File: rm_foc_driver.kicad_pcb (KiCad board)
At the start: 4 copper layers, 54.6 x 61.8 mm, 71 parts, among them J1 SWD, J2 SENSOR, J3 UART, J4 TMC4671, J5 PWM, J6 Conn_01x02, J7 CURRENT_SENSE, J8 Conn_01x03, Q1 IRF7580M, Q2 IRF7580M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

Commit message: Not complete yet
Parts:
- removed C1 (x2): 10uF, Capacitor_SMD:C_0603_1608Metric
- removed C14, C18, C19, C20: 100nF, Capacitor_SMD:C_0603_1608Metric
- removed C17: 1uF, Capacitor_SMD:C_0603_1608Metric
- removed C21: 2.2nF, Capacitor_SMD:C_0603_1608Metric
- removed J7: CURRENT_SENSE, Connector_PinHeader_2.54mm:PinHeader_1x02_P2.54mm_Vertical
- removed U5: AS5047D, Package_SO:TSSOP-14_4.4x5mm_P0.65mm
- added D4: DIODE, Diode_SMD:D_SMA, F.Cu at (169.3, 100.8)
- added D5: DIODE, Diode_SMD:D_SMA, F.Cu at (164.5, 100.8)
- added D6: DIODE, Diode_SMD:D_SMA, F.Cu at (159.6, 100.9)
- added R12: 200k, Resistor_SMD:R_0603_1608Metric, F.Cu at (80.9, 157.8)
- added R13: 10R, Resistor_SMD:R_0603_1608Metric, F.Cu at (156.2, 94.0)
- added R14: 10R, Resistor_SMD:R_0603_1608Metric, F.Cu at (162.1, 94.0)
- added R15: 10R, Resistor_SMD:R_0603_1608Metric, F.Cu at (152.4, 94.0)
- added R16: 10R, Resistor_SMD:R_0603_1608Metric, F.Cu at (160.0, 94.0)
- added R17: 10R, Resistor_SMD:R_0603_1608Metric, F.Cu at (148.6, 93.9)
- added R18: 10R, Resistor_SMD:R_0603_1608Metric, F.Cu at (158.1, 94.0)
- added U6: INA2180, Package_SO:VSSOP-8_3.0x3.0mm_P0.65mm, F.Cu at (169.4, 93.4)
- added U7: MT6701, Package_SO:SOP-8_3.9x4.9mm_P1.27mm, B.Cu at (165.1, 101.0)
- C10: value 1uF -> 100nF; moved to F.Cu
- C12, C13: value 1uF -> 100nF
- C15: value 2.2uF -> 1uF
- C16: value 4.7uF -> 1uF; footprint Capacitor_SMD:C_0805_2012Metric -> Capacitor_SMD:C_0603_1608Metric
- C2, C24, C25, C26, C27, C29, C30, C31, C32, C33, C34, C35, C36, C37: moved to F.Cu
- R9: value 1R -> 200k
- U4: value DRV8303 -> EG2133; footprint Package_SO:TSSOP-48_6.1x12.5mm_P0.5mm -> Package_SO:TSSOP-20_4.4x6.5mm_P0.65mm
- moved J1 143.9 mm to (45.6, 152.0), turned to 0 degrees
- moved C32 134.3 mm to (54.8, 176.0), turned to 0 degrees
- moved C27 124.9 mm to (50.4, 176.0), turned to 0 degrees
- moved C34 122.6 mm to (59.1, 174.2)
- moved J2 122.1 mm to (28.1, 170.2), turned to 0 degrees
- moved J4 121.3 mm to (32.8, 152.8), turned to 0 degrees
- moved C24 119.4 mm to (37.3, 161.1), turned to 0 degrees
- moved C16 116.5 mm to (59.1, 176.8), turned to 0 degrees
- moved J3 115.3 mm to (60.9, 135.1), turned to 0 degrees
- moved D2 112.3 mm to (59.6, 168.5), turned to 0 degrees
- moved C31 112.2 mm to (68.2, 163.7), turned to 0 degrees
- moved C25 111.6 mm to (58.4, 171.5), turned to 0 degrees
- moved D1 111.4 mm to (63.6, 168.5), turned to 0 degrees
- moved Y1 109.3 mm to (76.8, 153.8), turned to 0 degrees
- moved C33 106.8 mm to (70.1, 151.7), turned to 0 degrees
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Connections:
- C10 pad 1: +3.3V -> Net-(C10-Pad1)
- C10 pad 2: GND -> /SH_A
- C12 pad 2: GND -> /SH_B
- C13 pad 2: GND -> /SH_C
- C15 pad 1: GND -> +5V
- C15 pad 2: Net-(C15-Pad2) -> GND
- C16 pad 1: +12V -> +5V
- R9 pad 1: Net-(R9-Pad1) -> +5V
- R9 pad 2: GND -> Net-(R9-Pad2)
- U4 pad 1: unconnected-(U4-Pad1) -> /PWM1
- U4 pad 12: /EN_GATE -> /SH_A
- U4 pad 13: /PWM1 -> Net-(U4-Pad13)
- U4 pad 14: /PWM2 -> Net-(C10-Pad1)
- U4 pad 15: /PWM3 -> /SH_B
- U4 pad 16: /PWM4 -> Net-(U4-Pad16)
- U4 pad 17: /PWM5 -> Net-(C12-Pad1)
- U4 pad 18: /PWM6 -> /SH_C
- U4 pad 19: Net-(C12-Pad1) -> Net-(U4-Pad19)
- U4 pad 2: unconnected-(U4-Pad2) -> /PWM2
- U4 pad 20: +3.3V -> Net-(C13-Pad1)
- U4 pad 3: Net-(R9-Pad1) -> /PWM3
- U4 pad 4: /CS1 -> /PWM4
- U4 pad 5: /MOSI -> /PWM5
- U4 pad 6: /MISO -> /PWM6
- U4 pad 7: /SCLK -> +5V
- U4 pad 8: /DC_CAL -> GND
- U4 pad 9: Net-(C15-Pad2) -> Net-(U4-Pad9)
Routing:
- net +3.3V: track 121.5 -> 0.00 mm, vias 7 -> 0
- net +5V: track 114.5 -> 32.0 mm, vias 4 -> 1
- net GND: track 66.1 -> 0.00 mm, vias 58 -> 0
- net /SCLK: track 64.6 -> 0.00 mm, vias 2 -> 0
- net /MISO: track 61.8 -> 0.00 mm, vias 2 -> 0
- net /MOSI: track 57.5 -> 0.00 mm, vias 2 -> 0
- net /CS1: track 47.3 -> 0.00 mm, vias 2 -> 0
- net /Encoder_I: track 41.9 -> 0.00 mm
- net /Encoder_B: track 36.7 -> 0.00 mm
- net /Encoder_A: track 35.7 -> 0.00 mm
- net /SL_A: track 34.0 -> 0.00 mm, vias 22 -> 24
- net /DC_CAL: track 33.7 -> 0.00 mm, vias 2 -> 0
- net /SWDIO: track 27.7 -> 0.00 mm, vias 2 -> 0
- net /EN_GATE: track 27.7 -> 0.00 mm, vias 2 -> 0
- net Net-(D1-Pad1): track 26.3 -> 0.00 mm
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- added copper zone on B.Cu, net /SL_A
- added copper zone on B.Cu, net /SL_B
- removed copper zone on B.Cu, net +12V
- removed copper zone on B.Cu, net /SH_A
- removed copper zone on In1.Cu, net /SH_A
- removed copper zone on B.Cu, net /SH_B
- removed copper zone on In1.Cu, net /SH_B
- removed copper zone on B.Cu, net /SH_C
- removed copper zone on In1.Cu, net /SH_C
- removed copper zone on B.Cu, net GND
- removed copper zone on F.Cu, net GND
- removed copper zone on In1.Cu, net GND
- removed copper zone on In2.Cu, net GND
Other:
- board size 54.6 x 61.8 mm -> 70 x 70 mm

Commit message: new verson of pcb.ready to print
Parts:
- removed J2: SENSOR, Connector_PinHeader_2.54mm:PinHeader_1x03_P2.54mm_Vertical
- removed R12, R9: 200k, Resistor_SMD:R_0603_1608Metric
- C16: moved to B.Cu
- D3, D4, D5, D6: footprint Diode_SMD:D_SMA -> Diode_SMD:D_SOD-123
- moved C32 143.3 mm to (170.2, 91.0), turned to -90 degrees
- moved C27 135.1 mm to (155.5, 91.1), turned to -90 degrees
- moved C24 132.7 mm to (150.1, 91.1), turned to -90 degrees
- moved C15 131.9 mm to (178.9, 108.8), turned to -90 degrees
- moved C16 130.8 mm to (164.6, 99.4), turned to 180 degrees
- moved D2 122.1 mm to (172.1, 121.3), turned to 180 degrees
- moved C31 121.5 mm to (165.6, 91.0), turned to -90 degrees
- moved C34 120.3 mm to (168.5, 124.3), turned to 180 degrees
- moved C25 120.0 mm to (147.6, 91.1), turned to -90 degrees
- moved D1 119.7 mm to (172.2, 118.2), turned to 180 degrees
- moved J4 118.3 mm to (148.6, 128.7), turned to -128 degrees
- moved J1 118.1 mm to (161.5, 129.8), turned to -90 degrees
- moved C33 115.1 mm to (167.9, 91.0), turned to -90 degrees
- moved J3 113.9 mm to (174.7, 130.0), turned to -90 degrees
- moved C29 113.6 mm to (157.9, 91.1), turned to -90 degrees
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- renumbered C22 to C
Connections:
- C11 pad 1: /OSC_IN -> /OSC_OUT
- C9 pad 1: /OSC_OUT -> /OSC_IN
- J4 pad 4: /CS3 -> /CS2
- U3 pad 18: unconnected-(U3-Pad18) -> /ADC1
- U3 pad 19: unconnected-(U3-Pad19) -> /MODE
- U3 pad 29: /CS3 -> unconnected-(U3-Pad29)
- U7 pad 2: Net-(R9-Pad2) -> /MODE
- U7 pad 3: unconnected-(U7-Pad3) -> /ADC1
- U7 pad 6: unconnected-(U7-Pad6) -> /MISO
- U7 pad 7: unconnected-(U7-Pad7) -> /SCLK
- U7 pad 8: Net-(R12-Pad1) -> /CS1
- Y1 pad 1: /OSC_OUT -> /OSC_IN
- Y1 pad 3: /OSC_IN -> /OSC_OUT
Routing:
- net +3.3V: track 0.00 -> 94.1 mm, vias 0 -> 6
- net +5V: track 32.0 -> 115.0 mm, vias 1 -> 8
- net /SL_A: track 0.00 -> 51.1 mm, vias 24 -> 16
- net /SCLK: track 0.00 -> 50.2 mm
- net /MISO: track 0.00 -> 50.2 mm
- net /SL_B: track 0.00 -> 42.8 mm, vias 24 -> 16
- net GND: track 0.00 -> 37.6 mm, vias 0 -> 74
- net /GL_C: track 0.00 -> 33.7 mm, vias 0 -> 2
- net /MODE: track 0.00 -> 28.2 mm, vias 0 -> 2
- net /ADC1: track 0.00 -> 27.3 mm, vias 0 -> 2
- net /GL_B: track 0.00 -> 27.0 mm, vias 0 -> 2
- net /CS1: track 0.00 -> 25.5 mm, vias 0 -> 1
- net /SWDIO: track 0.00 -> 20.8 mm, vias 0 -> 1
- net /GL_A: track 14.7 -> 35.1 mm, vias 1 -> 2
- net /SWCLK: track 0.00 -> 18.4 mm, vias 0 -> 1
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- added copper zone on B.Cu, net GND
- added copper zone on F.Cu, net GND
- added copper zone on In1.Cu, net GND
- added copper zone on In2.Cu, net GND
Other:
- board text added: "+5V"
- board text added: "2022/8/10"
- board text added: "CLK"
- board text added: "CS2"
- board text added: "DIO"
- board text added: "DynamicX"
- board text added: "GND"
- board text added: "MISO"
- board text added: "MOSI"
- board text added: "PWM1"
- board text added: "PWM2"
- board text added: "PWM3"
- board text added: "PWM4"
- board text added: "PWM5"
- board text added: "PWM6"
- board text added: "RXD"
- board text added: "SCK"
- board text added: "TXD"
- board text added: "VCC"
- board text added: "cyl0411"

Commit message: Update pcb-layout.Not complete yet.Current progress 50%.
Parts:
- C24, C25, C26, C27, C29, C30, C31, C32, C33: moved to B.Cu
- moved C22 28.9 mm to (189.7, 50.5)
- moved U2 19.1 mm to (194.2, 91.6), turned to 145 degrees
- moved C2 18.7 mm to (195.5, 88.9), turned to 145 degrees
- moved C15 16.0 mm to (171.3, 94.7)
- moved U6 16.0 mm to (166.6, 94.7)
- moved C32 15.4 mm to (154.8, 90.5)
- moved C27 11.0 mm to (166.5, 90.5)
- moved C33 10.8 mm to (157.1, 90.5)
- moved R10 7.37 mm to (147.3, 79.0)
- moved C26 7.35 mm to (152.5, 90.5)
- moved R11 7.32 mm to (157.6, 79.0)
- moved C31 6.25 mm to (159.4, 90.5)
- moved C29 6.18 mm to (164.1, 90.5)
- moved C16 5.77 mm to (162.8, 104.9)
- moved U7 3.58 mm to (165.1, 101.0)
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- renumbered C to C22
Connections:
- U3 pad 11: /DC_CAL -> unconnected-(U3-Pad11)
- U3 pad 12: /EN_GATE -> unconnected-(U3-Pad12)
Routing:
- net +5V: track 115.0 -> 18.1 mm, vias 8 -> 1
- net +3.3V: track 94.1 -> 0.00 mm, vias 6 -> 0
- net /SCLK: track 50.2 -> 0.00 mm
- net /MISO: track 50.2 -> 0.00 mm
- net GND: track 37.6 -> 3.81 mm, vias 74 -> 27
- net /GL_C: track 33.7 -> 63.3 mm
- net /GL_B: track 27.0 -> 54.5 mm
- net /CS1: track 25.5 -> 0.00 mm, vias 1 -> 0
- net /SH_B: track 23.2 -> 48.0 mm, vias 3 -> 52
- net Net-(C7-Pad2): track 24.0 -> 0.00 mm
- net /MODE: track 28.2 -> 5.72 mm, vias 2 -> 0
- net /SH_A: track 23.3 -> 45.5 mm, vias 2 -> 52
- net /SWDIO: track 20.8 -> 0.00 mm, vias 1 -> 0
- net /ADC1: track 27.3 -> 6.87 mm, vias 2 -> 0
- net /SWCLK: track 18.4 -> 0.00 mm, vias 1 -> 0
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- added copper zone on In1.Cu, net /SH_A
- added copper zone on In2.Cu, net /SH_A
- added copper zone on In1.Cu, net /SH_B
- added copper zone on In2.Cu, net /SH_B
- added copper zone on In1.Cu, net /SH_C
- added copper zone on In2.Cu, net /SH_C
- removed copper zone on B.Cu, net GND
- removed copper zone on F.Cu, net GND
- removed copper zone on In1.Cu, net GND
- removed copper zone on In2.Cu, net GND

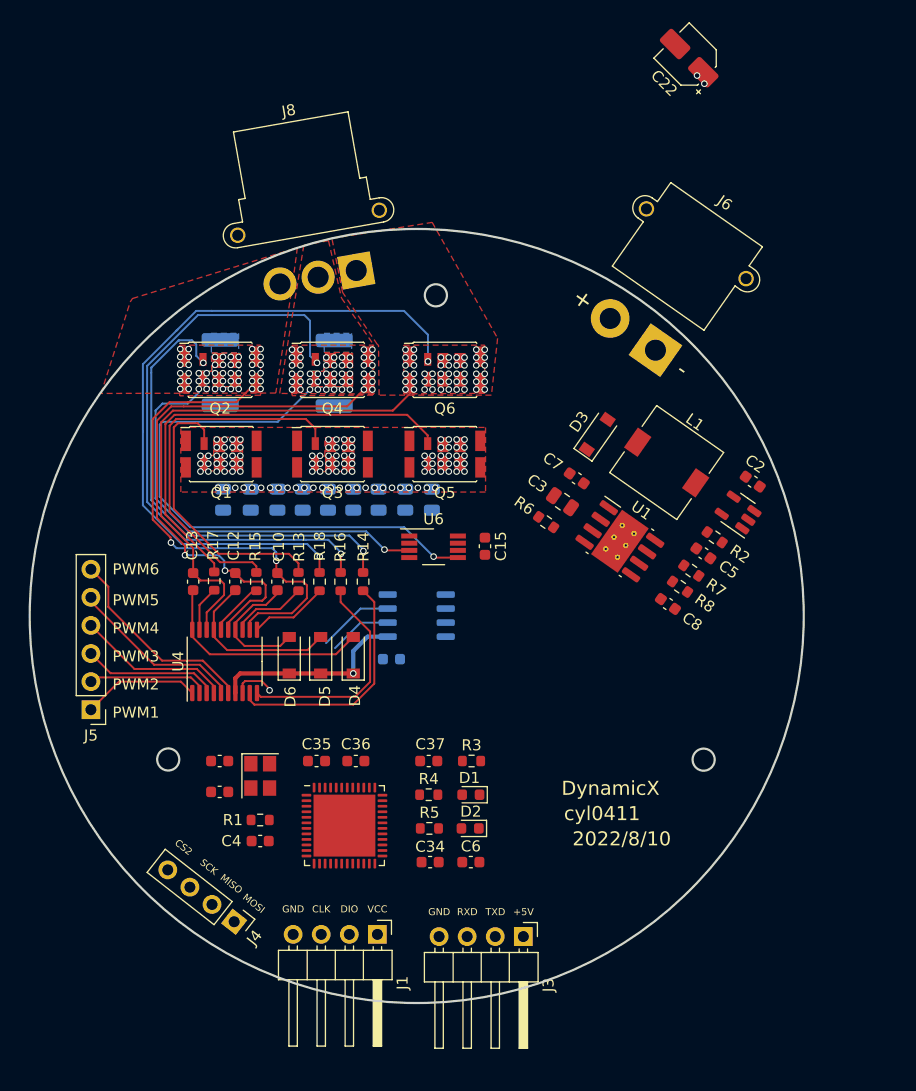
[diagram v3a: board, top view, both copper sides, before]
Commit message: Straight line version.
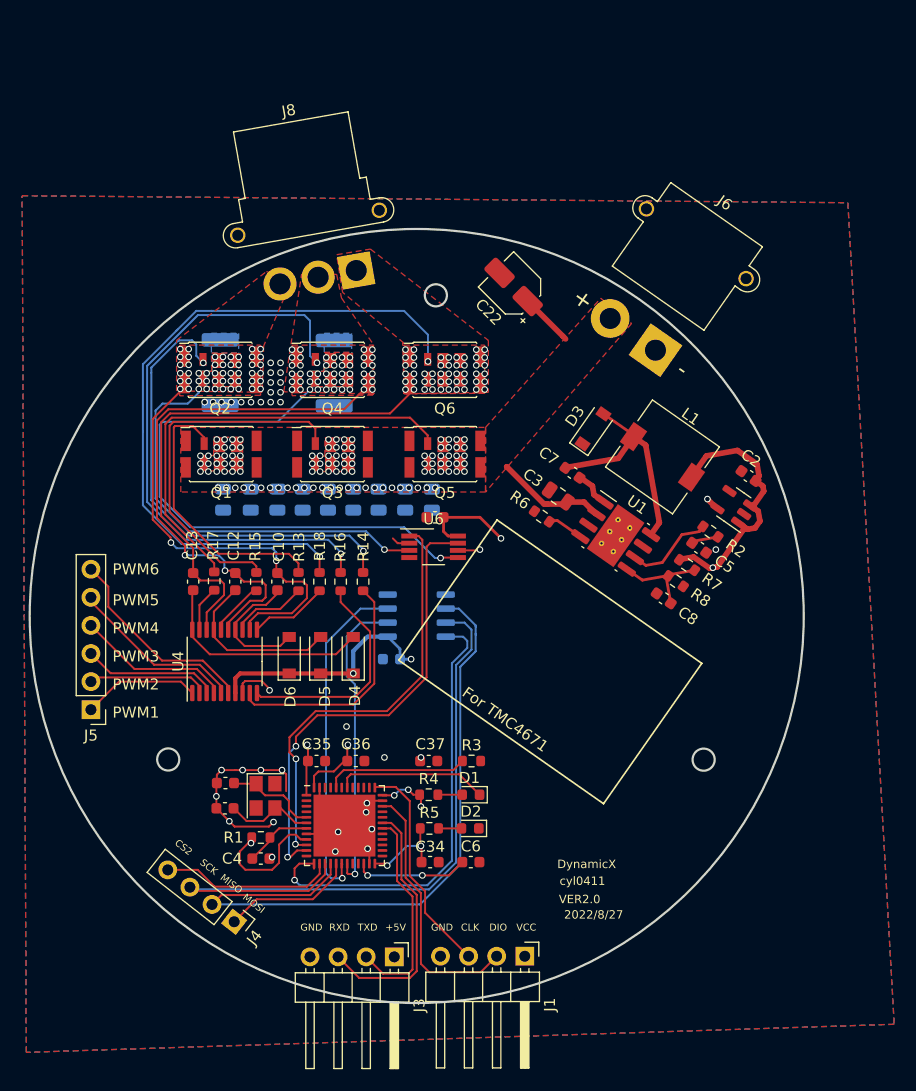
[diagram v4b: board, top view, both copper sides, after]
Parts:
- moved C22 26.1 mm to (173.9, 71.2)
- moved J1 13.5 mm to (174.9, 131.8)
- moved J3 11.8 mm to (163.1, 131.8)
- moved C15 5.22 mm to (166.8, 92.1), turned to 180 degrees
- moved C9 2.06 mm to (147.8, 116.1)
- moved Y1 1.87 mm to (151.4, 117.3)
- moved C4 1.58 mm to (151.0, 122.9)
- moved R1 1.58 mm to (151.0, 121.0)
- moved C11 1.56 mm to (147.8, 118.4)
- moved D3 0.64 mm to (181.0, 84.1)
- moved U1 0.64 mm to (183.1, 93.7)
- moved R6 0.64 mm to (176.4, 92.0)
- moved R8 0.64 mm to (188.5, 97.8)
- moved C2 0.63 mm to (195.1, 88.3)
- moved C3 0.63 mm to (177.9, 90.2)
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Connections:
- U3 pad 10: unconnected-(U3-Pad10) -> /SO1
- U3 pad 11: unconnected-(U3-Pad11) -> /SO2
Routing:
- net +3.3V: track 0.00 -> 155.2 mm, vias 0 -> 10
- net +5V: track 18.1 -> 158.9 mm, vias 1 -> 4
- net /SCLK: track 0.00 -> 63.3 mm
- net /MISO: track 0.00 -> 62.4 mm
- net /SO2: track 0.00 -> 42.0 mm, vias 0 -> 2
- net /CS1: track 0.00 -> 41.4 mm, vias 0 -> 1
- net /SO1: track 0.00 -> 38.9 mm, vias 0 -> 2
- net GND: track 3.81 -> 41.6 mm, vias 27 -> 62
- net /SWDIO: track 0.00 -> 23.9 mm
- net /ADC1: track 6.87 -> 30.8 mm, vias 0 -> 1
- net /RXD: track 0.00 -> 23.3 mm
- net /MODE: track 5.72 -> 27.6 mm, vias 0 -> 1
- net Net-(C7-Pad2): track 0.00 -> 20.5 mm
- net /SWCLK: track 0.00 -> 19.9 mm
- net /TXD: track 0.00 -> 19.3 mm
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- added copper zone on B.Cu, net GND
- added copper zone on F.Cu, net GND
- added copper zone on In1.Cu, net GND
- added copper zone on In2.Cu, net GND
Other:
- board text added: "2022/8/27"
- board text added: "For TMC4671"
- board text added: "VER2.0"
- board text removed: "2022/8/10"

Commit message: Fcuk IRF7580 fuck fuck.csd18540 is better
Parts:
- J5: value PWM -> Conn_01x07; footprint Connector_PinHeader_2.54mm:PinHeader_1x06_P2.54mm_Vertical -> Connector_PinHeader_2.54mm:PinHeader_1x07_P2.54mm_Vertical
- Q1, Q2, Q3, Q4, Q5, Q6: value IRF7580M -> CSD18540Q5B; footprint Package_DirectFET:DirectFET_ME -> Package_TO_SOT_SMD:TDSON-8-1
- moved R11 7.86 mm to (150.9, 83.1)
- moved R10 6.75 mm to (142.2, 83.4)
- moved Q5 6.14 mm to (161.5, 87.1), turned to -90 degrees
- moved Q6 5.89 mm to (161.8, 79.5)
- moved Q3 4.01 mm to (153.5, 87.1), turned to -90 degrees
- moved Q4 3.76 mm to (153.8, 79.5)
- moved C24 3.72 mm to (143.9, 90.8)
- moved C25 3.72 mm to (146.4, 90.8)
- moved C29 3.72 mm to (160.4, 90.8)
- moved C26 3.72 mm to (148.8, 90.8)
- moved C27 3.72 mm to (162.8, 90.8)
- moved C30 3.72 mm to (157.9, 90.8)
- moved C31 3.72 mm to (155.7, 90.8)
- moved C32 3.72 mm to (151.1, 90.8)
- moved C33 3.72 mm to (153.4, 90.8)
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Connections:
- Q1 pad 1: +12V -> /SH_A
- Q1 pad 2: /GH_A -> /SH_A
- Q2 pad 1: /SH_A -> /SL_A
- Q2 pad 2: /GL_A -> /SL_A
- Q3 pad 1: +12V -> /SH_B
- Q3 pad 2: /GH_B -> /SH_B
- Q4 pad 1: /SH_B -> /SL_B
- Q4 pad 2: /GL_B -> /SL_B
- Q5 pad 1: +12V -> /SH_C
- Q5 pad 2: /GH_C -> /SH_C
- Q6 pad 1: /SH_C -> GND
- Q6 pad 2: /GL_C -> GND
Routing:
- net /GL_C: track 63.3 -> 17.0 mm
- net /GL_B: track 54.5 -> 20.0 mm
- net /SL_B: track 50.7 -> 29.8 mm, vias 27 -> 16
- net /GL_A: track 42.1 -> 25.4 mm
- net /GH_C: track 40.6 -> 31.1 mm, vias 0 -> 2
- net /SH_C: track 46.9 -> 40.8 mm, vias 50 -> 53
- net /SH_B: track 48.0 -> 42.4 mm, vias 52 -> 50
- net GND: track 41.6 -> 45.6 mm, vias 62 -> 72
- net /GH_A: track 25.3 -> 21.6 mm
- net +12V: track 14.9 -> 18.4 mm, vias 26 -> 15
- net /GH_B: track 33.2 -> 30.3 mm
- net /SH_A: track 39.2 -> 41.8 mm, vias 52 -> 49
- net /SL_A: track 37.8 -> 35.9 mm, vias 27 -> 16
- net /SO1: track 38.9 -> 39.4 mm
